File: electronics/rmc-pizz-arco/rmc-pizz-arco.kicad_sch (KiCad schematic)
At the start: 120 parts, among them J1 PZT, J2 PZT, J3 PZT, J4 PZT, J5 PZT, J6 PZT, J7 DIN-8, J8 PIZZ/ARCO, J9 9-15V DC, U1 OPA2191, U10 CD4066B, U2 OPA2191, U3 OPA2191, U4 OPA2191, U5 OPA2191, U6 OPA2191, U7 OPA2191, U8 CD4066B, U9 CD4066B

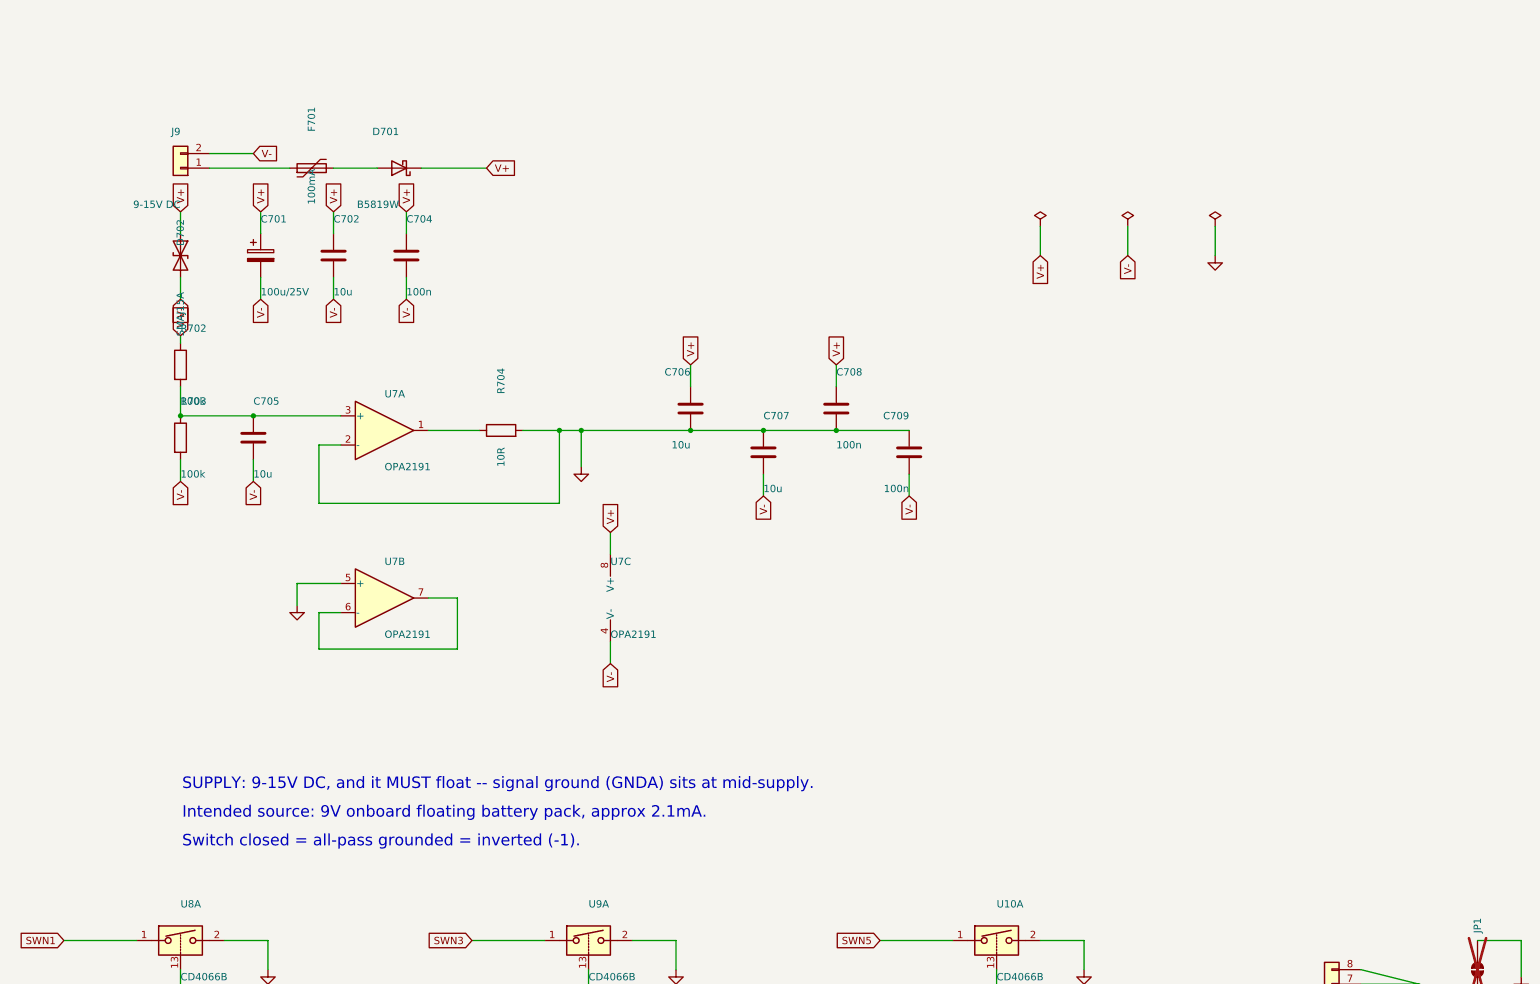
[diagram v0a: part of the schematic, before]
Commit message: Supersede: bipolar +/-9V charge-pump board with onboard battery
Complete and self-consistent -- verify.py matches the schematic to design.py exactly (58 nets, 322 pin connections) and the board lays out at 56 x 94 mm with DRC nearly clean. Kept as a record of the +/-9V exploration only.

Superseded by RMC's reply of 2026-07-30: the board takes bipolar power from the Poly-Drive II over DIN-8 pins 7 and 8 with the shell as ground, so there is no battery, no charge pump and no power section. See electronics/STATE.md.
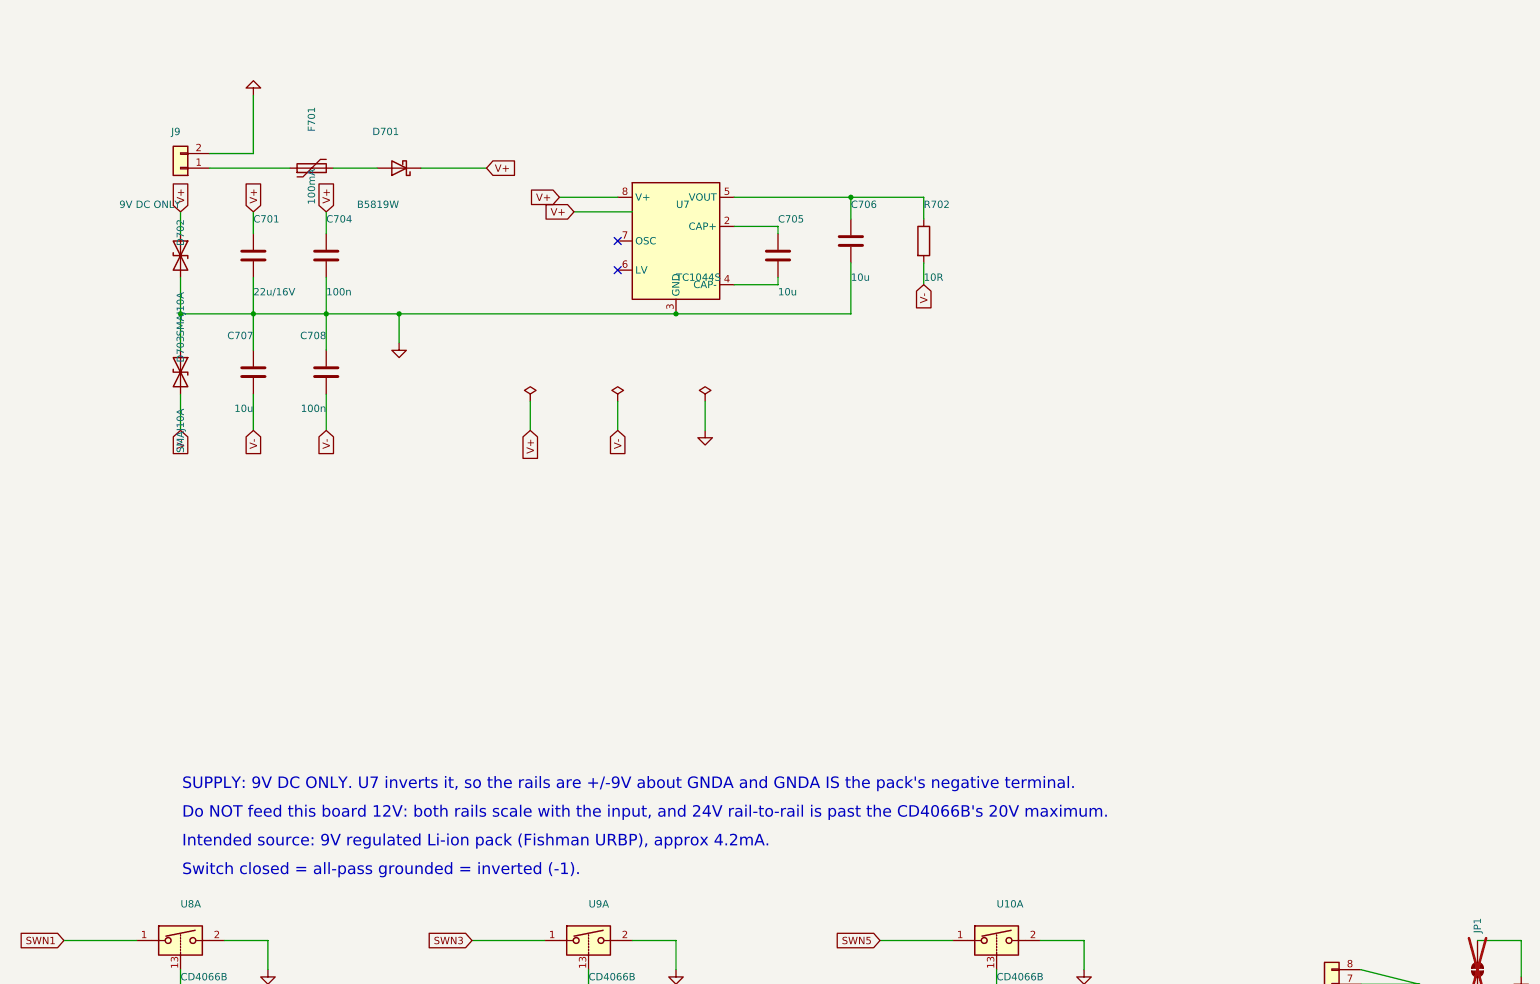
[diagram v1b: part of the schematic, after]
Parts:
- removed C702: 10u, Capacitor_SMD:C_0805_2012Metric, symbol Device:C
- removed C709: 100n, Capacitor_SMD:C_0805_2012Metric, symbol Device:C
- removed R703: 100k, Resistor_SMD:R_0805_2012Metric, symbol Device:R
- removed R704: 10R, Resistor_SMD:R_0805_2012Metric, symbol Device:R
- removed unit 2 of U7
- removed unit 3 of U7
- added D703: SMAJ10A, Diode_SMD:D_SMA, symbol Device:D_TVS
- C102, C103, C104, C105, C106, C107, C202, C203, C204, C205, C206, C207, C302, C303, C304, C305, C306, C307, C402, C403, C404, C405, C406, C407, C502, C503, C504, C505, C506, C507, C602, C603, C604, C605, C606, C607, C703, C704, C705, C706, C707, C708, C801, C802, C803, C804, C805, C806: footprint Capacitor_SMD:C_0805_2012Metric -> Capacitor_SMD:C_0402_1005Metric
- C701: value 100u/25V -> 22u/16V; footprint Capacitor_SMD:CP_Elec_6.3x5.4 -> Capacitor_SMD:C_1210_3225Metric; symbol Device:C_Polarized -> Device:C
- D702: value SMAJ15A -> SMAJ10A
- J1, J2, J3, J4, J5, J6: footprint Connector_PinHeader_2.54mm:PinHeader_1x03_P2.54mm_Vertical -> Connector_JST:JST_SH_BM03B-SRSS-TB_1x03-1MP_P1.00mm_Vertical
- J7: footprint Connector_PinHeader_2.54mm:PinHeader_1x08_P2.54mm_Vertical -> Connector_JST:JST_SH_BM08B-SRSS-TB_1x08-1MP_P1.00mm_Vertical
- J8: footprint Connector_PinHeader_2.54mm:PinHeader_1x02_P2.54mm_Vertical -> Connector_JST:JST_SH_BM02B-SRSS-TB_1x02-1MP_P1.00mm_Vertical
- J9: value 9-15V DC -> 9V DC ONLY; footprint Connector_PinHeader_2.54mm:PinHeader_1x02_P2.54mm_Vertical -> Connector_JST:JST_SH_BM02B-SRSS-TB_1x02-1MP_P1.00mm_Vertical
- R103, R104, R105, R106, R203, R204, R205, R206, R303, R304, R305, R306, R403, R404, R405, R406, R503, R504, R505, R506, R603, R604, R605, R606, R701: footprint Resistor_SMD:R_0805_2012Metric -> Resistor_SMD:R_0402_1005Metric
- R702: value 100k -> 10R; footprint Resistor_SMD:R_0805_2012Metric -> Resistor_SMD:R_0402_1005Metric
- U10, U8, U9: footprint Package_SO:SO-14_3.9x8.65mm_P1.27mm -> Package_SO:TSSOP-14_4.4x5mm_P0.65mm
- U7: value OPA2191 -> TC1044S; symbol rmc:OPA2191 -> rmc:TC1044S
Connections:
- net AGND: now also C701.2, C704.2, C706.2, C707.2, D702.2 (A2), J9.2 (Pin_2), U7.3 (GND), D703.1 (A1); no longer C706.1, C707.1, U7.2 (-)
- net V+: now also U7.1 (BOOST), U7.8 (V+); no longer C706.2, C708.1, R702.1
- net V-: now also C707.1, C708.1, R702.2, D703.2 (A2); no longer C701.2, C704.2, C705.2, C707.2, D702.2 (A2), J9.2 (Pin_2)
- new net: C706.1, R702.1, U7.5 (VOUT)
- new net: C705.1, U7.2 (CAP+)
- new net: C705.2, U7.4 (CAP-)
- no-connect marks 0 -> 2
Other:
- note added: "Do NOT feed this board 12V: both rails scale with the input, and 24V rail-to-rail is past the CD4066B's 20V maximum."
- note added: "Intended source: 9V regulated Li-ion pack (Fishman URBP), approx 4.2mA."
- note added: "SUPPLY: 9V DC ONLY. U7 inverts it, so the rails are +/-9V about GNDA and GNDA IS the pack's negative terminal."
- note removed: "Intended source: 9V onboard floating battery pack, approx 2.1mA."
- note removed: "SUPPLY: 9-15V DC, and it MUST float -- signal ground (GNDA) sits at mid-supply."
- moved on the sheet: C704, C705, C706, C707, C708, R702
